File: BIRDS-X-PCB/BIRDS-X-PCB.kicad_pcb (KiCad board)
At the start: 2 copper layers, 85 x 85 mm, 87 parts, among them J101 LPC-50M2LG, J102 Conn_02x04_Odd_Even, J201 Conn_01x02, J202 Conn_01x02, J203 Conn_01x02, J401 Conn_01x04, J402 Conn_01x08, J403 Conn_01x02, J404 MHDR2X5, Q201 SI1470DH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

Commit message: Add silkscreen labels
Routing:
- net RFET_EN4: track 86.4 -> 85.8 mm
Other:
- board text added: "-"
- board text added: "12V,GND"
- board text added: "12uA->"
- board text added: "3V3"
- board text added: "3V3,GND"
- board text added: "3V3_EN"
- board text added: "5V"
- board text added: "5V,GND"
- board text added: "5V0"
- board text added: "5V_EN"
- board text added: "CLK"
- board text added: "CS"
- board text added: "GND"
- board text added: "HOLD/3"
- board text added: "MISO"
- board text added: "MOSI"
- board text added: "PA11/9"
- board text added: "PA12/10"
- board text added: "PA15"
- board text added: "RST"
- board text added: "RX"
- board text added: "SWDCLK"
- board text added: "SWDIO"
- board text added: "TX"
- board text added: "WP/IO2"
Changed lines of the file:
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@@
     (property "ki_keywords" "N-Channel MOSFET")
     (attr smd)
-    (fp_text reference "Q401" (at 0 -2.4 90) (layer "F.SilkS")
+    (fp_text reference "Q401" (at 2.4055 -1.474 -180) (layer "F.SilkS")
         (effects (font (size 1 1) (thickness 0.15)))
     )
@@
     (property "Sheetname" "PowerSheet")
     (attr through_hole)
-    (fp_text reference "U203" (at 7.62 -3.61 90) (layer "F.SilkS")
+    (fp_text reference "U203" (at 9.685 -3.325 90) (layer "F.SilkS")
         (effects (font (size 1 1) (thickness 0.15)))
     )
@@
     (property "ki_keywords" "R res resistor")
     (attr smd)
-    (fp_text reference "R410" (at 0 -1.65) (layer "F.SilkS")
+    (fp_text reference "R410" (at -1.07 -1.65) (layer "F.SilkS")
         (effects (font (size 1 1) (thickness 0.15)))
     )
@@
   (gr_line locked (start 50 135) (end 50 55)
     (stroke (width 0.1) (type default)) (layer "Edge.Cuts"))
-  (gr_text "Pin1" (at 66.2 123.9) (layer "F.SilkS")
+  (gr_text "5V0" (at 82 128.75 90) (layer "F.SilkS")
+    (effects (font (size 1 1) (thickness 0.15)) (justify right))
+  )
+  (gr_text "GND" (at 111.25 74) (layer "F.SilkS")
+    (effects (font (size 1 1) (thickness 0.15)) (justify left))
+  )
+  (gr_text "HOLD/3" (at 55 107.75) (layer "F.SilkS")
+    (effects (font (size 1 1) (thickness 0.15)) (justify left))
+  )
+  (gr_text "SWDCLK" (at 68 128.5 90) (layer "F.SilkS")
+    (effects (font (size 1 1) (thickness 0.15)) (justify right))
+  )
+  (gr_text "PA15" (at 98.28 74.58 270) (layer "F.SilkS")
+    (effects (font (size 1 1) (thickness 0.15)) (justify left))
+  )
+  (gr_text "CLK" (at 55 105.25) (layer "F.SilkS")
+    (effects (font (size 1 1) (thickness 0.15)) (justify left))
+  )
+  (gr_text "SWDIO" (at 68 125 90) (layer "F.SilkS")
+    (effects (font (size 1 1) (thickness 0.15)) (justify left))
+  )
+  (gr_text "GND" (at 80 125 90) (layer "F.SilkS")
+    (effects (font (size 1 1) (thickness 0.15)) (justify left))
+  )
+  (gr_text "5V,GND" (at 87 115.5) (layer "F.SilkS")
+    (effects (font (size 1 1) (thickness 0.15)) (justify left))
+  )
+  (gr_text "-" (at 68.5825 115.945 90) (layer "F.SilkS")
+    (effects (font (size 1 1) (thickness 0.15)) (justify bottom))
+  )
+  (gr_text "3V3" (at 92 124.75 90) (layer "F.SilkS")
+    (effects (font (size 1 1) (thickness 0.15)) (justify left))
+  )
+  (gr_text "PA11/9" (at 68.75 122.25) (layer "F.SilkS")
+    (effects (font (size 1 1) (thickness 0.15)) (justify left bottom))
+  )
+  (gr_text "RX" (at 84 125 90) (layer "F.SilkS")
+    (effects (font (size 1 1) (thickness 0.15)) (justify left))
+  )
+  (gr_text "WP/IO2" (at 55 97.75) (layer "F.SilkS")
+    (effects (font (size 1 1) (thickness 0.15)) (justify left))
+  )
+  (gr_text "3V3" (at 55 110.25) (layer "F.SilkS")
+    (effects (font (size 1 1) (thickness 0.15)) (justify left))
+  )
+  (gr_text "MISO" (at 55 95.25) (layer "F.SilkS")
+    (effects (font (size 1 1) (thickness 0.15)) (justify left))
+  )
+  (gr_text "5V0" (at 82 125 90) (layer "F.SilkS")
+    (effects (font (size 1 1) (thickness 0.15)) (justify left))
+  )
+  (gr_text "TX" (at 84 128.75 90) (layer "F.SilkS")
+    (effects (font (size 1 1) (thickness 0.15)) (justify right))
+  )
+  (gr_text "PA12/10" (at 95.71 74.58 270) (layer "F.SilkS")
+    (effects (font (size 1 1) (thickness 0.15)) (justify left))
+  )
+  (gr_text "GND" (at 55 100) (layer "F.SilkS")
+    (effects (font (size 1 1) (thickness 0.15)) (justify left))
+  )
+  (gr_text "3V3,GND" (at 87 111.5) (layer "F.SilkS")
+    (effects (font (size 1 1) (thickness 0.15)) (justify left))
+  )
+  (gr_text "-" (at 68.5825 109.165 90) (layer "F.SilkS")
+    (effects (font (size 1 1) (thickness 0.15)) (justify bottom))
+  )
+  (gr_text "RST" (at 69.75 124.5 45) (layer "F.SilkS")
+    (effects (font (size 1 1) (thickness 0.15)) (justify left))
+  )
+  (gr_text "CS" (at 55.051 92.456) (layer "F.SilkS")
+    (effects (font (size 1 1) (thickness 0.15)) (justify left))
+  )
+  (gr_text "5V" (at 111.25 79) (layer "F.SilkS")
+    (effects (font (size 1 1) (thickness 0.15)) (justify left))
+  )
+  (gr_text "-" (at 68.775 119.805 90) (layer "F.SilkS")
+    (effects (font (size 1 1) (thickness 0.15)) (justify bottom))
+  )
+  (gr_text "-" (at 68.5825 112.555 90) (layer "F.SilkS")
+    (effects (font (size 1 1) (thickness 0.15)) (justify bottom))
+  )
+  (gr_text "12uA->" (at 80.25 52.25) (layer "F.SilkS")
     (effects (font (size 1 1) (thickness 0.15)) (justify left bottom))
   )
+  (gr_text "3V3_EN" (at 86 124.75 45) (layer "F.SilkS")
+    (effects (font (size 1 1) (thickness 0.15)) (justify left))
+  )
+  (gr_text "12V,GND" (at 86.765 119.13) (layer "F.SilkS")
+    (effects (font (size 1 1) (thickness 0.15)) (justify left))
+  )
+  (gr_text "MOSI" (at 55.051 102.646) (layer "F.SilkS")
+    (effects (font (size 1 1) (thickness 0.15)) (justify left))
+  )
+  (gr_text "5V_EN" (at 86 128.75 90) (layer "F.SilkS")
+    (effects (font (size 1 1) (thickness 0.15)) (justify right))
+  )
+  (gr_text "3V3" (at 92 128.75 90) (layer "F.SilkS")
+    (effects (font (size 1 1) (thickness 0.15)) (justify right))
+  )
+  (gr_text "Pin1" (at 67 126.5 90) (layer "F.SilkS")
+    (effects (font (size 1 1) (thickness 0.15)) (justify left bottom))
+  )
+  (gr_text "GND" (at 80 128.75 90) (layer "F.SilkS")
+    (effects (font (size 1 1) (thickness 0.15)) (justify right))
+  )
   (gr_text "(0,0) is (50,50)" (at 48.5 48.5) (layer "Dwgs.User")
     (effects (font (size 1 1) (thickness 0.15)) (justify left bottom))
@@
   (segment (start 67.5 81.5) (end 68 82) (width 0.25) (layer "B.Cu") (net 56))
   (segment (start 105 59.5) (end 104.25 59.5) (width 0.25) (layer "B.Cu") (net 56))
-  (segment (start 101.5 75) (end 90.75 75) (width 0.25) (layer "F.Cu") (net 57))
   (segment (start 103.701459 63.71) (end 103.661459 63.75) (width 0.25) (layer "F.Cu") (net 57))
   (segment (start 64.5 83.75) (end 64.25 83.5) (width 0.25) (layer "F.Cu") (net 57))
+  (segment (start 100.5 75) (end 90.75 75) (width 0.25) (layer "F.Cu") (net 57))
   (segment (start 57.724 83.5) (end 56.261 84.963) (width 0.25) (layer "F.Cu") (net 57))
   (segment (start 77.5 81.25) (end 79.497 81.25) (width 0.25) (layer "F.Cu") (net 57))
   (segment (start 64.25 83.5) (end 57.724 83.5) (width 0.25) (layer "F.Cu") (net 57))
+  (segment (start 101 74.5) (end 100.5 75) (width 0.25) (layer "F.Cu") (net 57))
   (segment (start 79.497 81.25) (end 79.613 81.134) (width 0.25) (layer "F.Cu") (net 57))
   (segment (start 103.661459 63.75) (end 101.5 63.75) (width 0.25) (layer "F.Cu") (net 57))
   (segment (start 104.39 63.71) (end 103.701459 63.71) (width 0.25) (layer "F.Cu") (net 57))
   (via (at 90.75 75) (size 0.8) (drill 0.4) (layers "F.Cu" "B.Cu") (net 57))
-  (via (at 101.5 75) (size 0.8) (drill 0.4) (layers "F.Cu" "B.Cu") (net 57))
+  (via (at 101 74.5) (size 0.8) (drill 0.4) (layers "F.Cu" "B.Cu") (net 57))
   (via (at 101.5 63.75) (size 0.8) (drill 0.4) (layers "F.Cu" "B.Cu") (net 57))
   (via (at 77.5 81.25) (size 0.8) (drill 0.4) (layers "F.Cu" "B.Cu") (net 57))
   (via (at 64.5 83.75) (size 0.8) (drill 0.4) (layers "F.Cu" "B.Cu") (net 57))
   (segment (start 64.5 83.75) (end 66.25 83.75) (width 0.25) (layer "B.Cu") (net 57))
-  (segment (start 101.5 63.75) (end 101.5 75) (width 0.25) (layer "B.Cu") (net 57))
   (segment (start 75.65 93.15) (end 79.372792 93.15) (width 0.25) (layer "B.Cu") (net 57))
+  (segment (start 101.5 63.75) (end 101.5 74) (width 0.25) (layer "B.Cu") (net 57))
   (segment (start 79.372792 93.15) (end 80.4 92.122792) (width 0.25) (layer "B.Cu") (net 57))
   (segment (start 66.25 83.75) (end 75.65 93.15) (width 0.25) (layer "B.Cu") (net 57))
@@
   (segment (start 80.475 76.525) (end 80.475 77.050305) (width 0.25) (layer "B.Cu") (net 57))
   (segment (start 80.050305 77.475) (end 79.4 77.475) (width 0.25) (layer "B.Cu") (net 57))
+  (segment (start 101.5 74) (end 101 74.5) (width 0.25) (layer "B.Cu") (net 57))
   (segment (start 90.75 75) (end 82 75) (width 0.25) (layer "B.Cu") (net 57))
   (segment (start 80.4 92.122792) (end 80.4 82.763604) (width 0.25) (layer "B.Cu") (net 57))

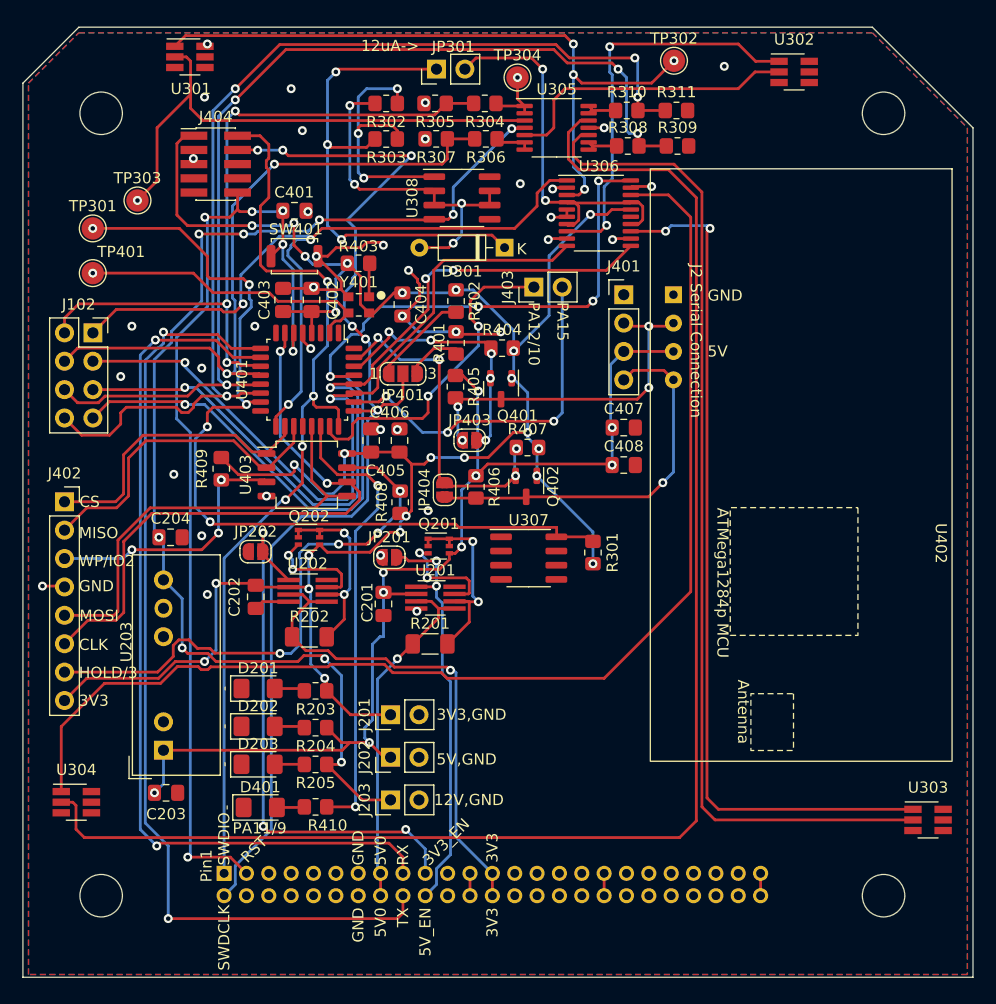
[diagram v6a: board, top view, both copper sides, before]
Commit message: Move 3v3 and 5v lines to polygon pour layers
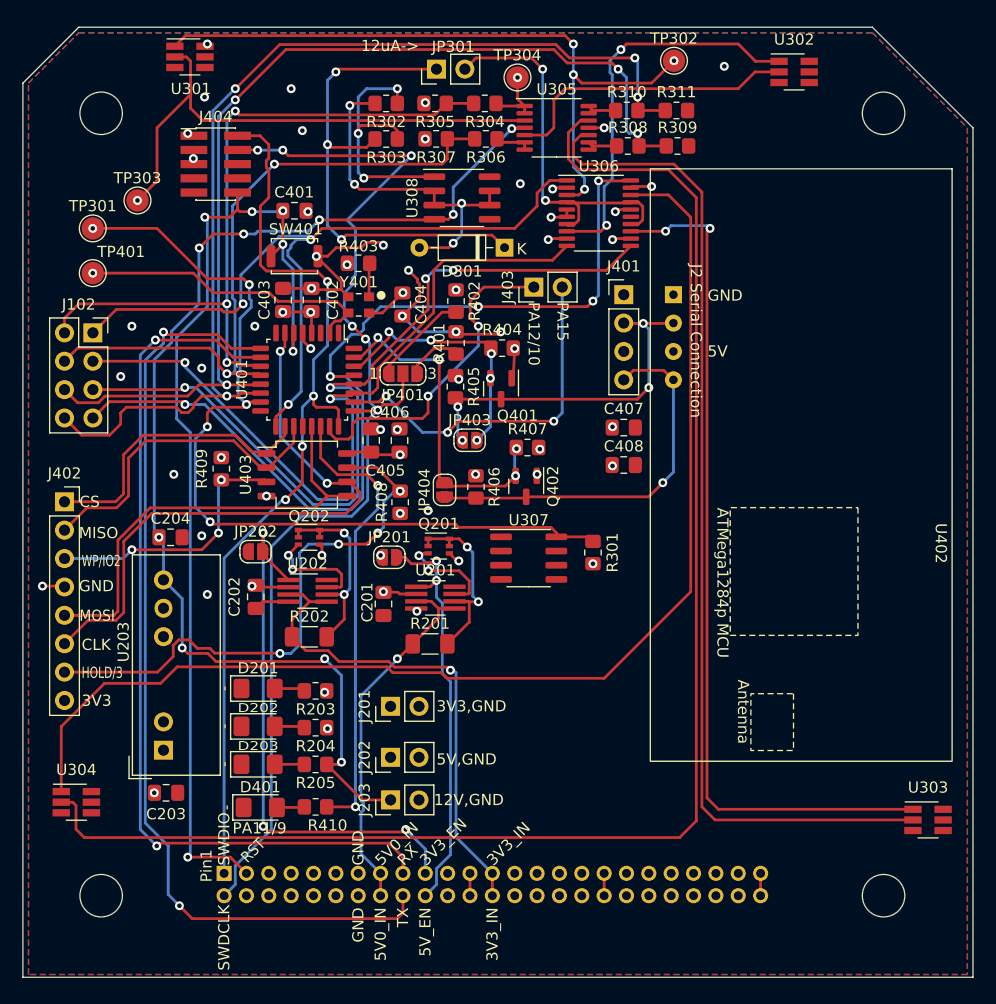
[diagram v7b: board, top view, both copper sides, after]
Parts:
- moved J201 0.75 mm to (82.9, 110.8)
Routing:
- net +3V3: track 201.8 -> 22.8 mm, vias 25 -> 17
- net +5V: track 100.2 -> 4.19 mm, vias 9 -> 8
- net SUP_5V0: track 31.8 -> 33.2 mm
- net TEMP_SENSE_1: track 80.1 -> 78.8 mm
- net UART_TX_JASPER_TO_BOSS: track 86.1 -> 84.9 mm
- net +12V: track 106.3 -> 105.1 mm
- net GND: track 48.5 -> 47.6 mm
- net Net-(U302-DIODE_ANODE): track 36.1 -> 35.4 mm
- net Net-(U201-SENSE): track 19.1 -> 18.5 mm
- net Net-(Q201-G): track 9.63 -> 9.10 mm
- added copper zone on In1.Cu, net +3V3
- added copper zone on In1.Cu, net +5V
- added copper zone on In2.Cu, net GND
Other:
- copper layers 2 -> 4
- board text added: "3V3_IN"
- board text added: "5V0_IN"
- board text removed: "5V0"

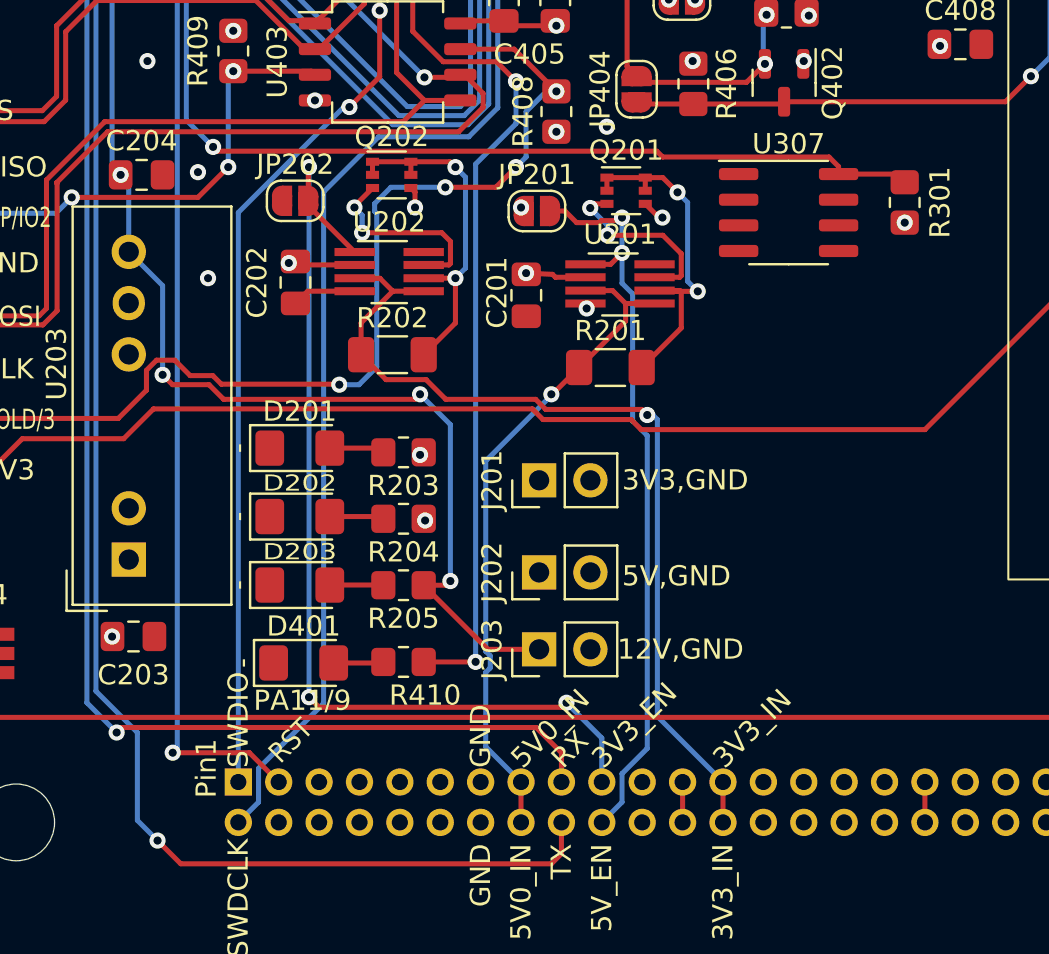
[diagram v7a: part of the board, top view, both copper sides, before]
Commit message: Re-route power lines from input to protection
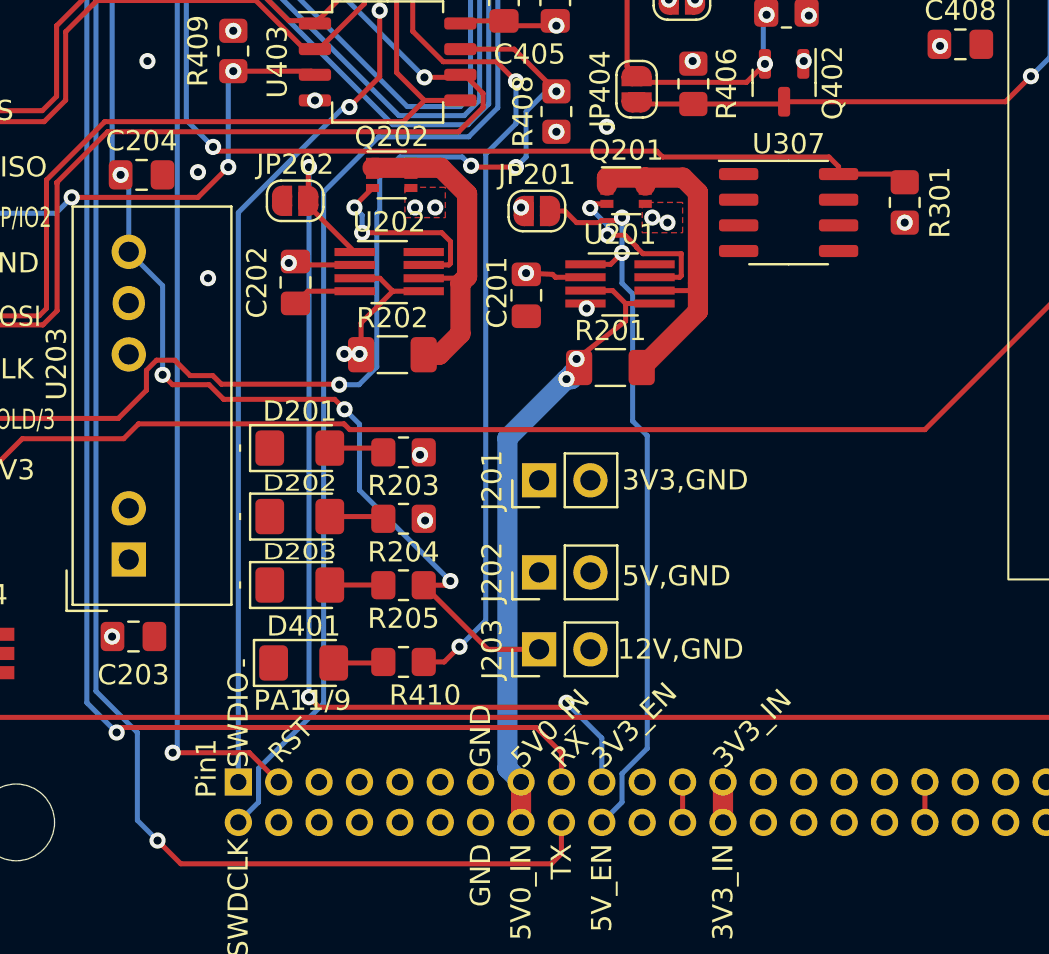
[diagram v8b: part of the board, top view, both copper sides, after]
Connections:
- net Net-(U201-SENSE) renamed /PowerSheet/5V_Current_Sense
- net Net-(U202-SENSE) renamed /PowerSheet/3V3_Current_Sense
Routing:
- net SUP_3V3_2: track 44.8 -> 69.6 mm, vias 1 -> 2
- net +12V: track 105.1 -> 102.3 mm
- net /PowerSheet/3V3_Current_Sense: track 17.4 -> 19.3 mm, vias 2 -> 0
- net Net-(U401-PA11/PA9): track 41.4 -> 40.2 mm
- net +5V: track 4.19 -> 3.06 mm, vias 8 -> 9
- net +3V3: track 22.8 -> 21.7 mm, vias 17 -> 18
- net Net-(J402-Pin_7): track 50.2 -> 51.1 mm
- net /PowerSheet/5V_Current_Sense: track 18.5 -> 17.7 mm, vias 2 -> 0
- net Net-(U304-DIODE_ANODE): track 107.7 -> 107.1 mm
- net SUP_5V0: track 33.2 -> 32.7 mm, vias 1 -> 2
- added copper zone on F.Cu, net +3V3
- added copper zone on F.Cu, net +5V
